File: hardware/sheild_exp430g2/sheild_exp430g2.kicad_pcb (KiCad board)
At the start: 2 copper layers, 57 x 50.8 mm, 28 parts, among them J1 Digital, J10 Conn_01x02_Male, J11 Conn_01x02_Male, J12 Conn_01x02_Male, J13 Conn_01x02_Male, J14 Conn_01x04_Male, J15 Conn_01x02_Male, J16 Conn_01x02_Male, J17 Conn_01x02_Male, J18 Conn_01x02_Male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

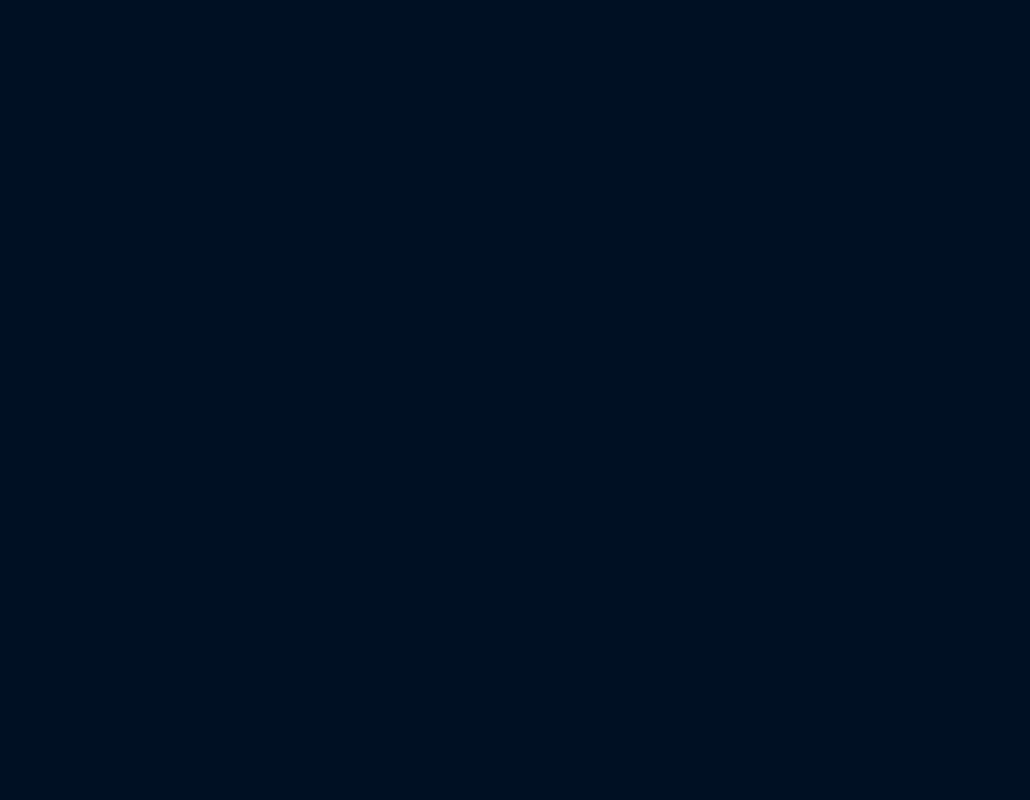
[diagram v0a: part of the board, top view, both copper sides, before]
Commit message: Added schematic pins
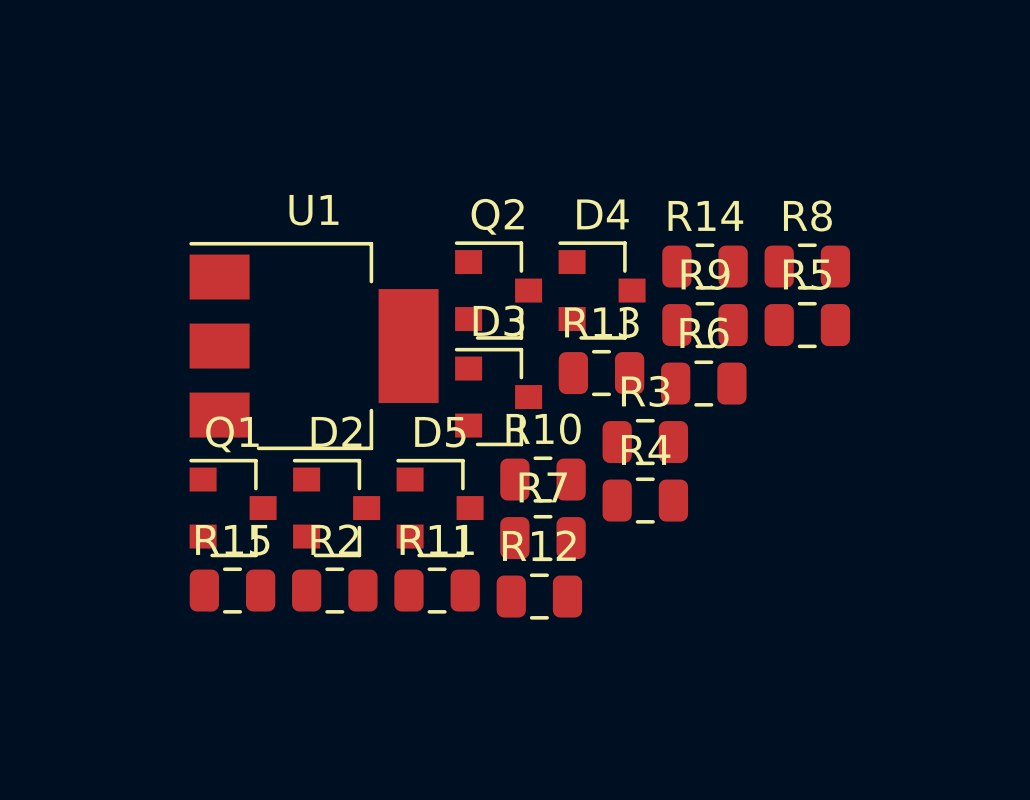
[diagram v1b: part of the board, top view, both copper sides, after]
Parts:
- added D2: BAT54S, Package_TO_SOT_SMD:SOT-23, F.Cu at (143.6, 104.2)
- added D3: BAT54S, Package_TO_SOT_SMD:SOT-23, F.Cu at (149.0, 100.5)
- added D4: BAT54S, Package_TO_SOT_SMD:SOT-23, F.Cu at (152.4, 96.9)
- added D5: BAT54S, Package_TO_SOT_SMD:SOT-23, F.Cu at (147.0, 104.2)
- added Q1: 2N7002, Package_TO_SOT_SMD:SOT-23, F.Cu at (140.1, 104.2)
- added Q2: 2N7002, Package_TO_SOT_SMD:SOT-23, F.Cu at (149.0, 96.9)
- added R10: 20K, Resistor_SMD:R_0805_2012Metric, F.Cu at (150.5, 103.2)
- added R11: 20K, Resistor_SMD:R_0805_2012Metric, F.Cu at (146.9, 106.9)
- added R12: 2k2, Resistor_SMD:R_0805_2012Metric, F.Cu at (150.3, 107.1)
- added R13: 2k2, Resistor_SMD:R_0805_2012Metric, F.Cu at (152.4, 99.7)
- added R14: 2k2, Resistor_SMD:R_0805_2012Metric, F.Cu at (155.9, 96.1)
- added R15: 2k2, Resistor_SMD:R_0805_2012Metric, F.Cu at (140.1, 106.9)
- added R2: 10k, Resistor_SMD:R_0805_2012Metric, F.Cu at (143.5, 106.9)
- added R3: 20K, Resistor_SMD:R_0805_2012Metric, F.Cu at (153.9, 102.0)
- added R4: 10k, Resistor_SMD:R_0805_2012Metric, F.Cu at (153.9, 103.9)
- added R5: 20K, Resistor_SMD:R_0805_2012Metric, F.Cu at (159.3, 98.1)
- added R6: 10k, Resistor_SMD:R_0805_2012Metric, F.Cu at (155.8, 100.0)
- added R7: 10k, Resistor_SMD:R_0805_2012Metric, F.Cu at (150.5, 105.2)
- added R8: 20K, Resistor_SMD:R_0805_2012Metric, F.Cu at (159.3, 96.1)
- added R9: 20K, Resistor_SMD:R_0805_2012Metric, F.Cu at (155.9, 98.1)
- added U1: AMS1117-3.3, Package_TO_SOT_SMD:SOT-223-3_TabPin2, F.Cu at (142.8, 98.8)
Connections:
- net Net-(J2-Pad4) renamed TEST
- net Net-(J2-Pad5) renamed RST
- J1 pad 10: Net-(J1-Pad10) -> P2.2
- J1 pad 2: Net-(J1-Pad2) -> P1.0
- J1 pad 4: Net-(J1-Pad4) -> P1.2
- J1 pad 5: Net-(J1-Pad5) -> P1.3
- J1 pad 6: Net-(J1-Pad6) -> P1.4
- J1 pad 7: Net-(J1-Pad7) -> P1.5
- J1 pad 8: Net-(J1-Pad8) -> P2.0
- J1 pad 9: Net-(J1-Pad9) -> P2.1
- J10 pad 2: 8 -> Net-(J10-Pad2)
- J11 pad 2: 7 -> P1.4
- J12 pad 2: 2 -> Net-(J12-Pad2)
- J13 pad 2: 4 -> P1.7
- J15 pad 2: 6 -> P2.1
- J16 pad 2: 5 -> P2.2
- J17 pad 2: 11 -> P2.4
- J18 pad 2: 3 -> P2.5
- J19 pad 2: A4(SDA) -> P2.0
- J2 pad 10: Net-(J2-Pad10) -> P2.3
- J2 pad 2: Net-(J2-Pad2) -> P2.6
- J2 pad 3: Net-(J2-Pad3) -> P2.7
- J2 pad 6: Net-(J2-Pad6) -> P1.7
- J2 pad 7: Net-(J2-Pad7) -> P1.6
- J2 pad 8: Net-(J2-Pad8) -> P2.5
- J2 pad 9: Net-(J2-Pad9) -> P2.4
- J20 pad 2: A5(SCL) -> P2.3
- J21 pad 2: 13 -> Net-(J21-Pad2)
- J24 pad 2: 12 -> Net-(J24-Pad2)
- J3 pad 1: ADC2 -> Net-(J3-Pad1)
- J3 pad 2: A0 -> +3V3
- J6 pad 2: A2 -> P1.0
- J7 pad 2: A1 -> P1.3
- J8 pad 1: ADC3 -> ADC2
- J8 pad 2: A3 -> ADC3

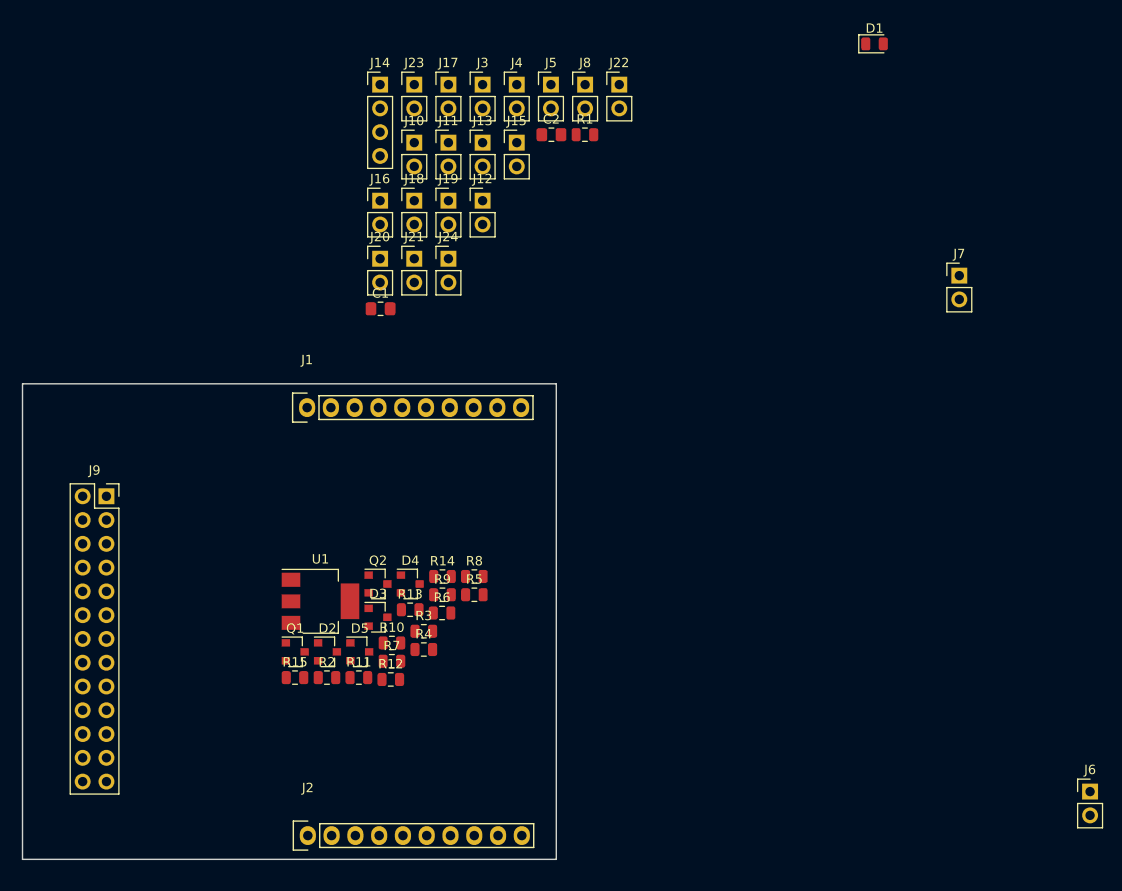
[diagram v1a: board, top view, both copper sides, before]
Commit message: Finish PCB layout
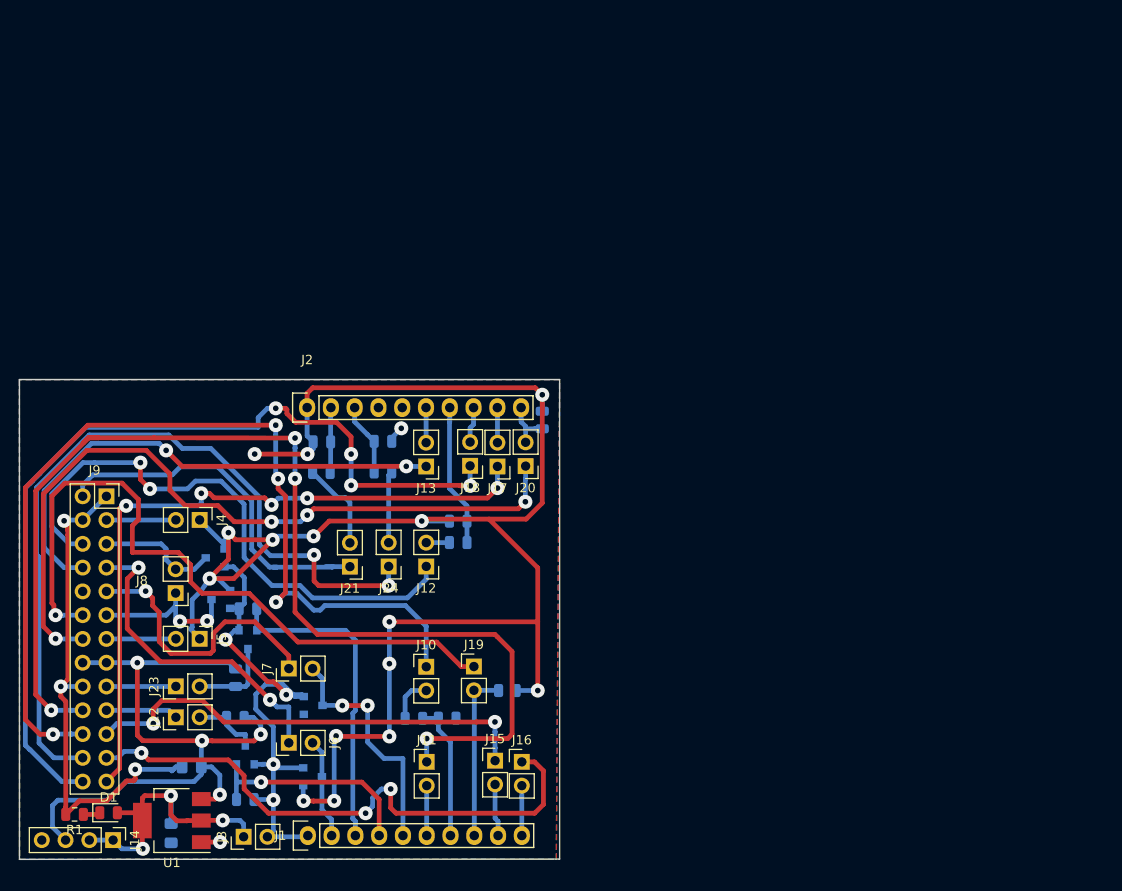
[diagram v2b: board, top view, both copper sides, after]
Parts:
- C1, C2, D2, D3, D4, D5, Q1, Q2, R10, R11, R12, R13, R14, R15, R2, R3, R4, R5, R6, R7, R8, R9: moved to B.Cu
- U1: value AMS1117-3.3 -> NCP1117-3.3_SOT223
- moved D1 115.9 mm to (120.2, 121.4)
- moved R1 90.8 mm to (116.6, 121.6), turned to 180 degrees
- moved J6 85.8 mm to (139.4, 113.9), turned to 90 degrees
- moved J14 85.6 mm to (120.7, 124.3), turned to 270 degrees
- moved C2 85.0 mm to (126.9, 123.6), turned to 270 degrees
- moved J3 84.3 mm to (134.6, 124.0), turned to 90 degrees
- moved J7 83.0 mm to (139.4, 106.0), turned to 90 degrees
- moved J22 82.5 mm to (127.4, 111.2), turned to 90 degrees
- moved J5 70.1 mm to (129.9, 102.8), turned to 270 degrees
- moved J8 69.7 mm to (127.4, 97.9), turned to 180 degrees
- moved J23 69.1 mm to (127.4, 107.9), turned to 90 degrees
- moved J11 66.2 mm to (154.2, 116.0)
- moved J15 66.1 mm to (161.5, 115.8)
- moved J16 61.8 mm to (164.3, 116.0)
- moved J4 57.5 mm to (129.9, 90.1), turned to 270 degrees
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- renumbered J2 to J1, J1 to J2
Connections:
- C2 pad 1: +3V3 -> Net-(C2-Pad1)
- D1 pad 2: +5V -> Net-(C2-Pad1)
- D4 pad 1: +3V3 -> GND
- D4 pad 2: Net-(D4-Pad2) -> +3V3
- D5 pad 1: +3V3 -> GND
- D5 pad 2: GND -> +3V3
- J1 pad 1: GND -> +3V3
- J1 pad 10: P2.3 -> P2.2
- J1 pad 2: P2.6 -> P1.0
- J1 pad 3: P2.7 -> P1.1
- J1 pad 4: TEST -> P1.2
- J1 pad 5: RST -> P1.3
- J1 pad 6: P1.7 -> P1.4
- J1 pad 7: P1.6 -> P1.5
- J1 pad 8: P2.5 -> P2.0
- J1 pad 9: P2.4 -> P2.1
- J14 pad 1: +5V -> Net-(C2-Pad1)
- J14 pad 2: +3V3 -> Net-(C2-Pad1)
- J2 pad 1: +3V3 -> GND
- J2 pad 10: P2.2 -> P2.3
- J2 pad 2: P1.0 -> P2.6
- J2 pad 3: Net-(J1-Pad3) -> P2.7
- J2 pad 4: P1.2 -> TEST
- J2 pad 5: P1.3 -> RST
- J2 pad 6: P1.4 -> P1.7
- J2 pad 7: P1.5 -> P1.6
- J2 pad 8: P2.0 -> P2.5
- J2 pad 9: P2.1 -> P2.4
- J3 pad 1: Net-(J3-Pad1) -> Net-(C2-Pad1)
- U1 pad 2: Net-(J3-Pad1) -> Net-(C2-Pad1)
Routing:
- net GND: track 0.00 -> 249.6 mm, vias 0 -> 20
- net Trig0: track 0.00 -> 123.7 mm, vias 0 -> 4
- net Echo0: track 0.00 -> 102.8 mm, vias 0 -> 4
- net PWM2N: track 0.00 -> 96.9 mm, vias 0 -> 4
- net D1: track 0.00 -> 86.1 mm, vias 0 -> 2
- net L_TCRT: track 0.00 -> 81.2 mm, vias 0 -> 4
- net R_TCRT: track 0.00 -> 75.6 mm, vias 0 -> 1
- net PWM2: track 0.00 -> 75.0 mm, vias 0 -> 5
- net +5V: track 0.00 -> 73.0 mm, vias 0 -> 4
- net Echo1: track 0.00 -> 62.2 mm, vias 0 -> 2
- net PWM1N: track 0.00 -> 61.1 mm, vias 0 -> 3
- net +3V3: track 0.00 -> 56.4 mm, vias 0 -> 4
- net Trig1: track 0.00 -> 55.0 mm, vias 0 -> 2
- net PWM1: track 0.00 -> 49.0 mm, vias 0 -> 2
- net D0: track 0.00 -> 39.2 mm
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- added copper zone on B.Cu, net GND
- added copper zone on F.Cu, net GND
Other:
- board size 57 x 50.8 mm -> 57.7 x 51.3 mm
- net class Default: clearance 0.2 -> 0.3048; trace_width 0.25 -> 0.508; via_dia 0.6 -> 1.5; via_drill 0.4 -> 0.6
- rule trace_clearance: 0.2 -> 0.3048
